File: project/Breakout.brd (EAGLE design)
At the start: 35.6 x 35.6 mm, 47 parts, among them J1 I2C1, J2 I2C2, J3 ER-TFT1.28-1, U1 SY8088, U15 ETA1611, U4 ESP32-S3-WROOM-1

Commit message: Layout complete
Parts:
- B1: value (none) -> RESET
- B2: value (none) -> BOOT
- C105: value 10uF/16V -> 2.2uF/16V
- C106: value 10uF/16V -> 4.7uF/16V
- D19: value 1A/23V/620mV -> (none); device SparkFun-DiscreteSemi:SOD-323 -> adafruit:SOD-523
- R126: value 10 -> 6.6
- U15: value ETA1611 -> BD60A60NUX; device discrete:SOT23-6 -> discrete:VSON008X2030
- moved C86 167.1 mm to (4.67, 26.7), turned to 180 degrees
- moved R74 156.2 mm to (5.99, 11.4)
- moved C19 152.3 mm to (6.70, 28.0), turned to 90 degrees
- moved C18 151.9 mm to (7.30, 31.2), turned to 180 degrees
- moved C17 146.9 mm to (7.00, 30.0), turned to 180 degrees
- moved D3 146.6 mm to (9.05, 11.4), turned to 90 degrees
- moved D2 144.3 mm to (8.00, 32.3), turned to 180 degrees
- moved C105 138.2 mm to (30.0, 32.2), turned to 135 degrees
- moved R13 136.5 mm to (7.78, 28.2), turned to 270 degrees
- moved R12 134.4 mm to (7.00, 30.0), flipped to the bottom, turned to 180 degrees
- moved C106 128.8 mm to (33.0, 24.5)
- moved C107 126.6 mm to (29.8, 27.4), turned to 90 degrees
- moved R126 122.5 mm to (30.8, 27.5), turned to 270 degrees
- moved R127 116.4 mm to (30.0, 25.0), turned to 90 degrees
- moved D19 103.2 mm to (32.0, 30.0), turned to 45 degrees
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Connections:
- removed net LCD_CTRL: R127.1
- removed net N$5: D19.A, L6.P$2, U15.1
- new net GPIO45: R127.1, U4.26
- new net LED_DIM: C107.1, R127.2, U15.3
- new net N$9: R126.2, U15.4
- net GND: now also U15.7, U15.PAD; no longer U15.2
- net GPIO48: now also U15.1
- net LED_A: now also D19.K, U15.6; no longer D19.C
- net LED_K: now also U15.5; no longer R126.2, U15.3
- net N$1: now also D19.A, L6.P$2, U15.8; no longer C107.1, R127.2, U15.4
- net USB_5V: now also U15.2; no longer U15.5
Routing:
- net MCU_VDD: track 0.00 -> 84.2 mm, vias 0 -> 4
- net GPIO48: track 0.00 -> 53.5 mm, vias 0 -> 2
- net USB_5V: track 0.00 -> 48.7 mm, vias 0 -> 3
- net GND: track 0.00 -> 36.8 mm, vias 0 -> 53
- net GPIO41: track 0.00 -> 27.7 mm, vias 0 -> 2
- net GPIO40: track 0.00 -> 27.4 mm, vias 0 -> 2
- net MCU_RST: track 0.00 -> 27.3 mm, vias 0 -> 2
- net GPIO0: track 0.00 -> 20.9 mm, vias 0 -> 2
- net USB_G: track 0.00 -> 19.8 mm
- net LED_A: track 0.00 -> 17.2 mm, vias 0 -> 2
- net GPIO45: track 0.00 -> 14.7 mm
- net GPIO7: track 0.00 -> 13.6 mm, vias 0 -> 1
- net USB_DN: track 0.00 -> 13.5 mm, vias 0 -> 1
- net USB_DP: track 0.00 -> 13.4 mm, vias 0 -> 1
- net GPIO6: track 0.00 -> 12.9 mm, vias 0 -> 1
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- added copper zone on layer 1, net GND
- added copper zone on layer 16, net GND
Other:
- board size 35.6 x 35.6 mm -> 38 x 38 mm

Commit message: cleanup and fixes
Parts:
- removed C107: 22pF/50V, rcl:C0402
- removed R127: 10, rcl:R0402
- removed TP2: (no value), SparkFun-Connectors:PAD.03X.03
- added C97: 0.1uF/6.3V, rcl:C0402
- added C98: 4.7uF/6.3V, rcl:C0402
- C86: value (none) -> 0.1uF/6.3V
- R126: value 6.6 -> 20K
- TP1: value (none) -> TPTP06R; device SparkFun-Connectors:PAD.03X.03 -> testpad:TP06R
- moved TP1 22.0 mm to (30.6, 30.7)
- moved R2 8.55 mm to (19.5, 9.60), turned to 180 degrees
- moved C1 8.50 mm to (19.5, 10.5), flipped to the bottom, turned to 0 degrees
- moved D12 6.93 mm to (33.4, 9.40)
- moved R3 5.56 mm to (19.5, 8.60), turned to 0 degrees
- moved R74 4.10 mm to (9.39, 9.15), turned to 180 degrees
- moved R126 3.49 mm to (29.2, 30.6), flipped to the bottom
- moved D19 2.24 mm to (33.0, 28.0), turned to 0 degrees
- moved L6 2.00 mm to (33.0, 25.0), flipped to the bottom, turned to 270 degrees
- moved C105 1.77 mm to (30.5, 30.5), turned to 270 degrees
- moved C4 1.70 mm to (29.2, 11.0), turned to 45 degrees
- moved C5 1.31 mm to (30.5, 10.2), turned to 45 degrees
- moved D2 1.30 mm to (7.90, 31.0)
- moved R1 1.23 mm to (18.1, 9.60), flipped to the top, turned to 270 degrees
- moved U15 1.10 mm to (30.5, 28.5), turned to 90 degrees
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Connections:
- removed net LED_DIM: C107.1, R127.2, U15.3
- net GND: now also B1.2, B2.2, C97.2, C98.2; no longer C107.2, TP2.1
- net GPIO0: now also B2.4
- net GPIO45: now also U15.3; no longer R127.1
- net LED_K: now also TP1.TP
- net MCU_RST: now also B1.4
- net MCU_VDD: now also C97.1, C98.1, U15.2; no longer TP1.1
- net USB_5V: no longer U15.2
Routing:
- net GPIO48: track 53.5 -> 35.1 mm
- net MCU_VDD: track 84.2 -> 95.3 mm, vias 4 -> 5
- net GPIO0: track 20.9 -> 11.6 mm
- net N$8: track 12.4 -> 4.04 mm, vias 2 -> 1
- net GND: track 36.8 -> 29.1 mm
- net LED_DIM: track 4.68 -> 0.00 mm, vias 1 -> 0
- net GPIO45: track 14.7 -> 19.2 mm, vias 0 -> 1
- net LED_A: track 17.2 -> 20.2 mm, vias 2 -> 1
- net USB_5V: track 48.7 -> 45.8 mm
- net LED_K: track 11.4 -> 14.2 mm
- net N$6: track 2.24 -> 4.63 mm, vias 1 -> 0
- net N$1: track 3.79 -> 5.25 mm
- net ESP_3V3: track 7.87 -> 9.11 mm
- net N$7: track 4.01 -> 5.22 mm
- net N$9: track 1.97 -> 0.91 mm, vias 1 -> 0
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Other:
- board text added: "5V"
- board text added: "BOOT"
- board text added: "I2C"
- board text added: "RST"

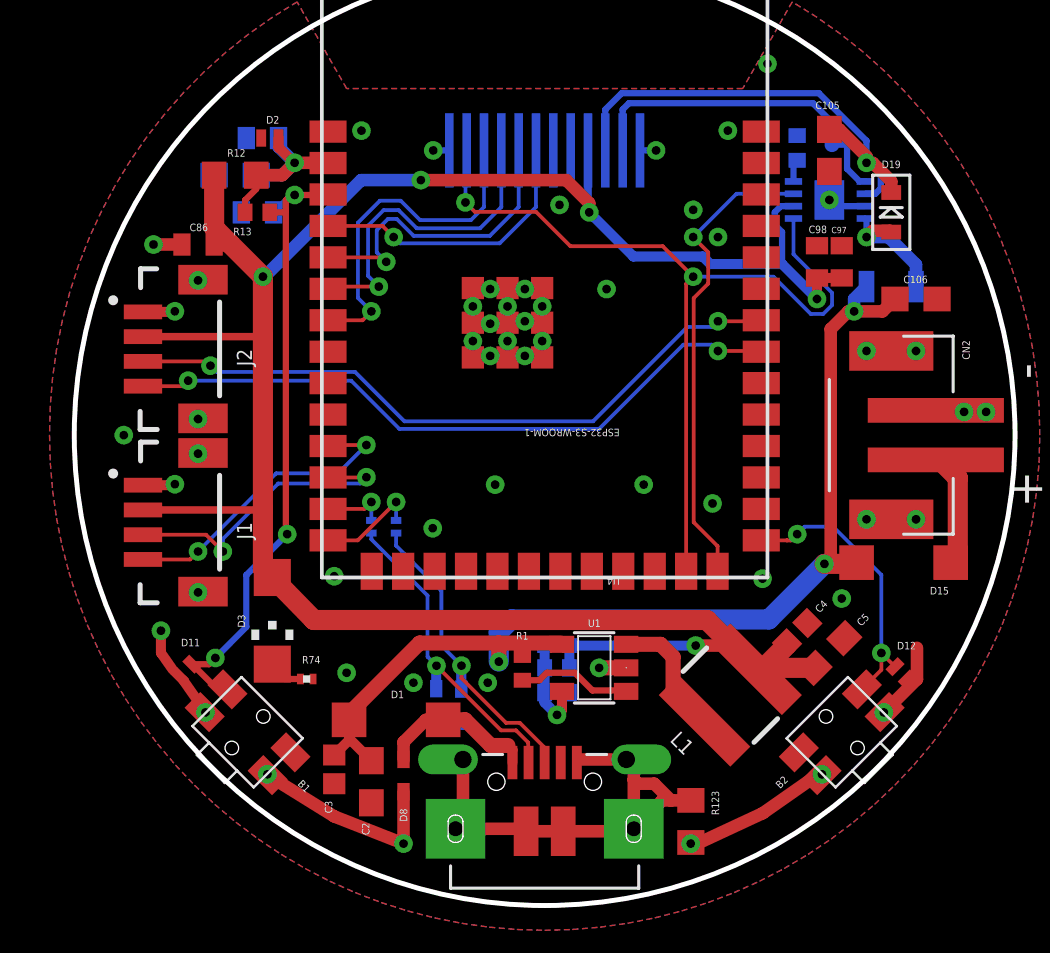
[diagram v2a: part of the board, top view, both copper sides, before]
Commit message: Display pinout fix
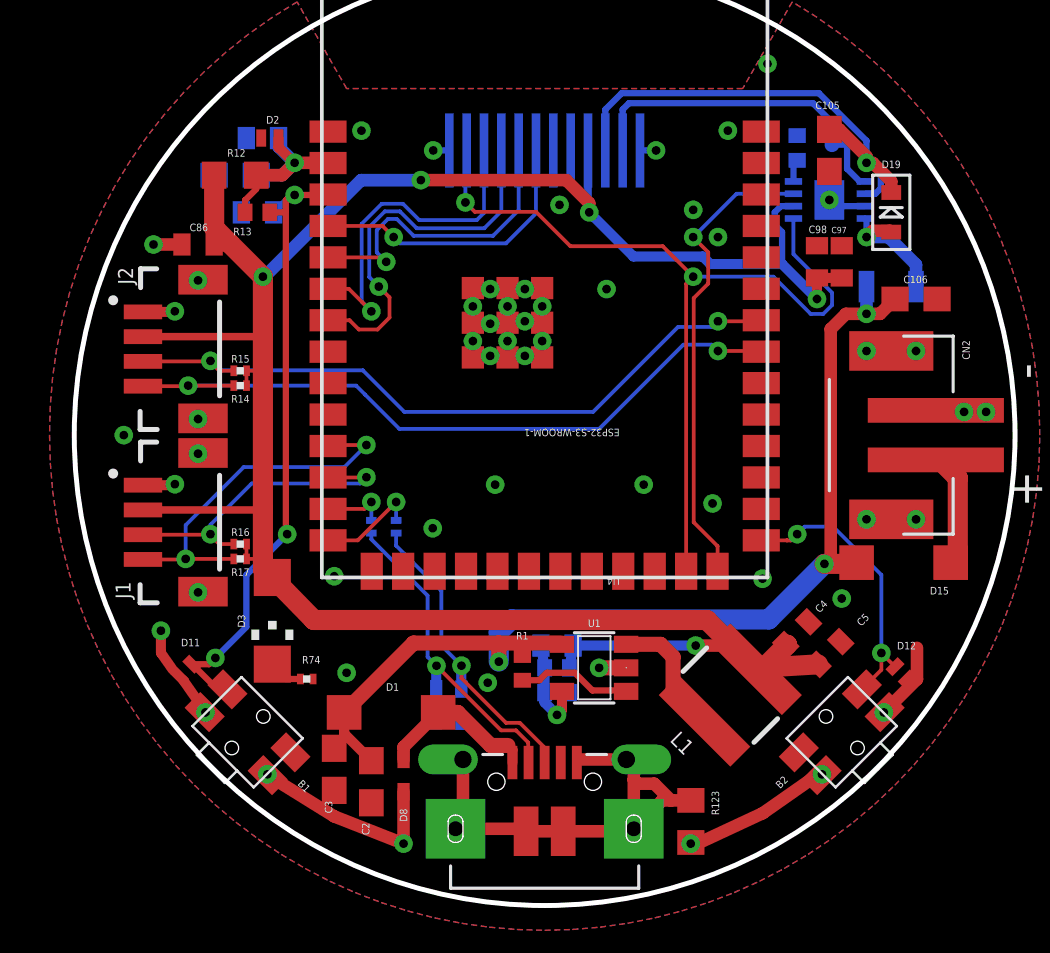
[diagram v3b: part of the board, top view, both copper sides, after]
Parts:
- added R14, R15: 4.7K, rcl:R0201
- added R16, R17: 1K, rcl:R0201
- C1: device SparkFun-Capacitors:0402-TIGHT -> rcl:C0402
- C2: device SparkFun-Capacitors:0603 -> rcl:C0603
- C3: device SparkFun-Capacitors:0402 -> rcl:C0603
- C4: device SparkFun-Capacitors:0402 -> rcl:C0402
- C5: device SparkFun-Capacitors:0603 -> rcl:C0402
- moved D1 0.36 mm to (12.8, 7.80)
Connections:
- net GPIO18: now also R17.2
- net GPIO40: now also R14.2
- net GPIO41: now also R15.2
- net GPIO6: now also J3.10; no longer J3.9
- net GPIO7: now also J3.9; no longer J3.10
- net GPIO8: now also R16.2
- net MCU_VDD: now also R14.1, R15.1, R16.1, R17.1
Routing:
- net GPIO18: track 12.5 -> 15.3 mm
- net MCU_VDD: track 95.3 -> 97.8 mm
- net GPIO40: track 27.4 -> 29.1 mm
- net GPIO7: track 14.0 -> 15.5 mm
- net GPIO41: track 27.7 -> 28.5 mm
- net GPIO6: track 13.3 -> 14.0 mm
- net GND: vias 53 -> 52
